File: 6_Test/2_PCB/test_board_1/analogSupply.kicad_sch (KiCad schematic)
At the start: 8 parts, among them U1 TPS74501PDRVR, U2 ADA4807-2ARMZ, U3 3310Y-001-103L

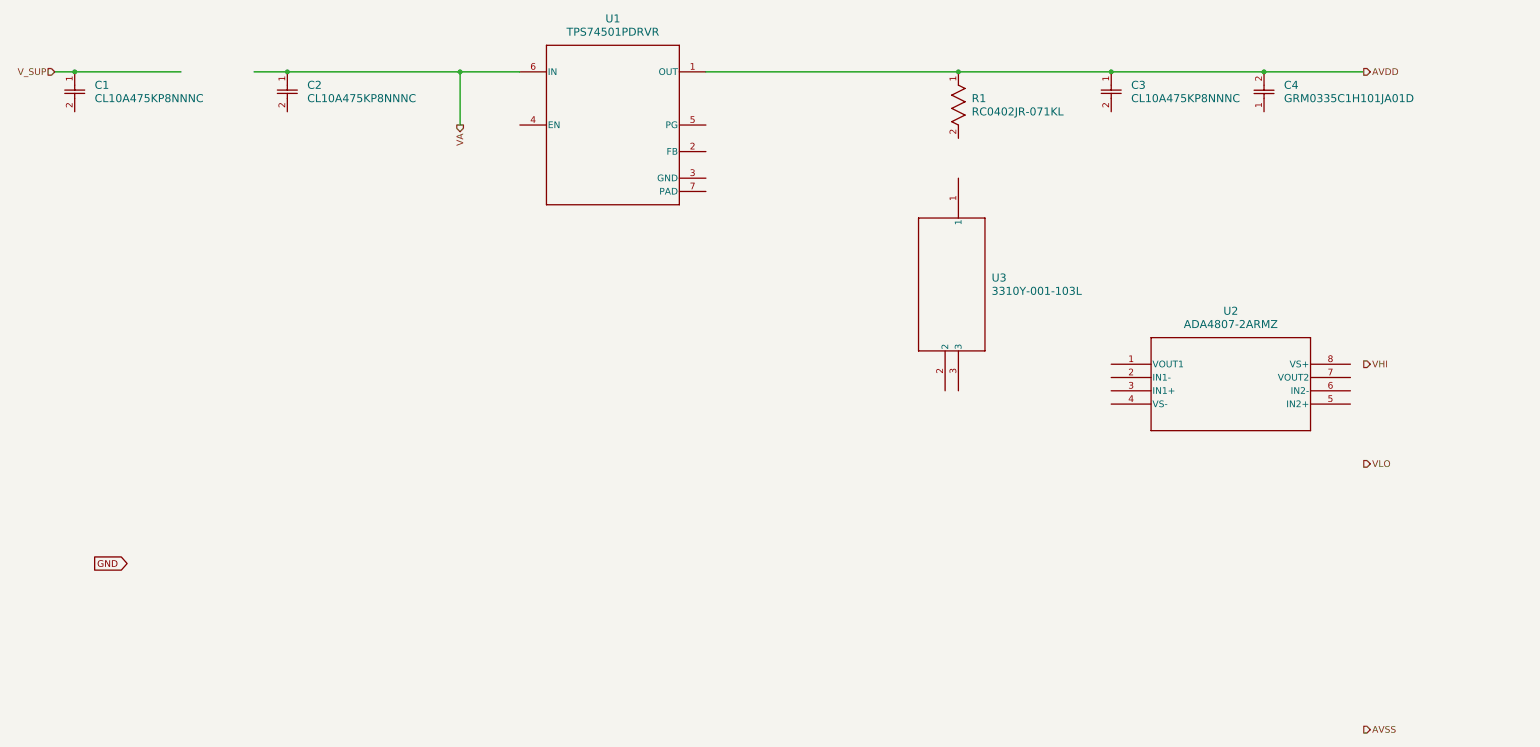
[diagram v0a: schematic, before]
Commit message: progress on analog supply
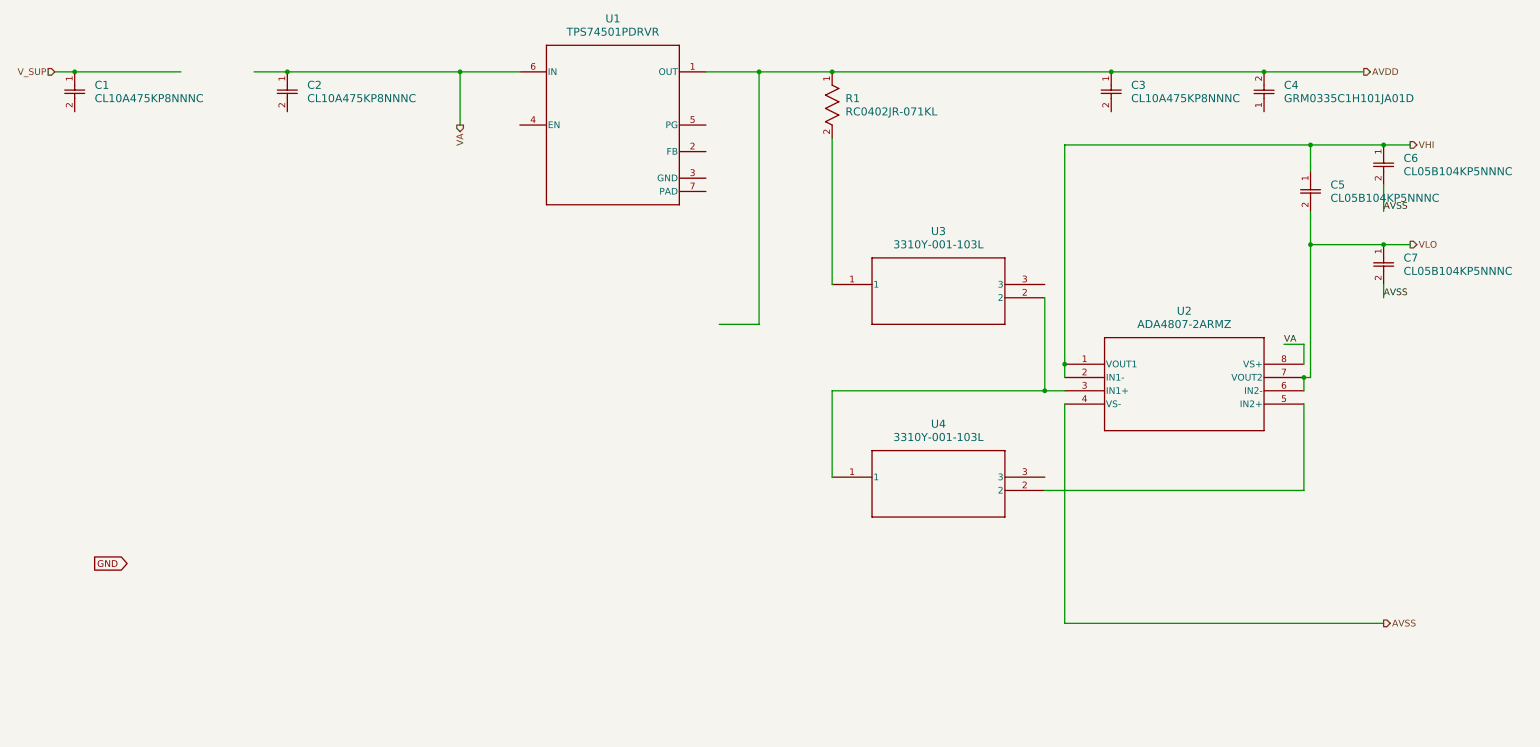
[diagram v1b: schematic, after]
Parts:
- added C5, C6, C7: CL05B104KP5NNNC, CAP_CL05_SAM, symbol cap100nF:CL05B104KP5NNNC
- added U4: 3310Y-001-103L, TO_3310Y, symbol potentiometer:3310Y-001-103L
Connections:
- net AVSS: now also U2.4 (VS-), C6.2, C7.2
- net VA: now also U2.8 (VS+)
- net VHI: now also U2.1 (VOUT1), U2.2 (IN1-), C5.1, C6.1
- net VLO: now also U2.6 (IN2-), U2.7 (VOUT2), C5.2, C7.1
- net at U3.1: now also R1.2
- net at U3.2: now also U2.3 (IN1+), U4.1
- net at U2.5 (IN2+): now also U4.2
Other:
- moved on the sheet: R1, U2, U3

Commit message: progress on analog supply. added ferrite beads
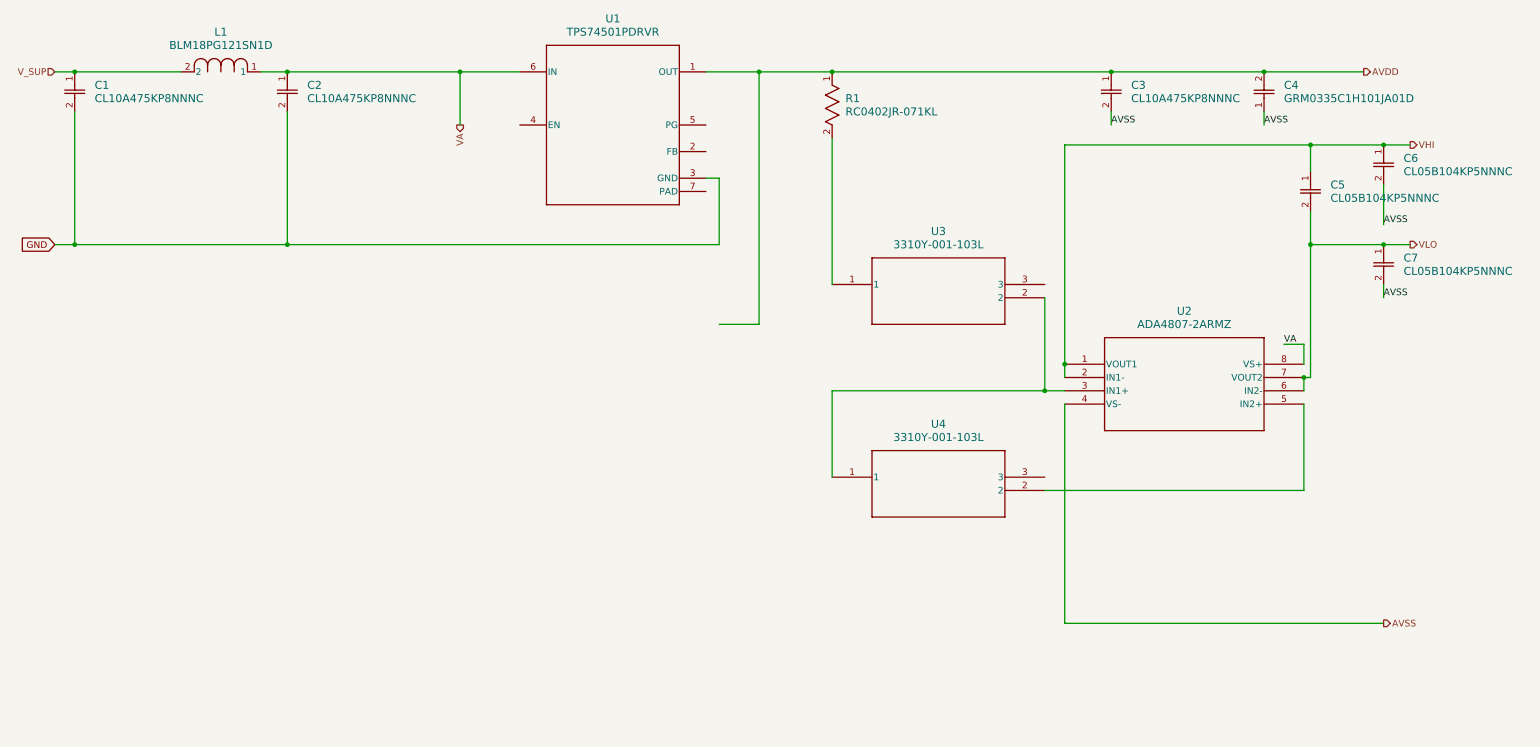
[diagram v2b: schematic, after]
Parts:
- added L1: BLM18PG121SN1D, IND_BLM18_0603_MUR, symbol ferriteBeads120Ohm:BLM18PG121SN1D
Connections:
- net AVSS: now also C3.2, C4.1
- net GND: now also C1.2, C2.2, U1.3 (GND)
- net VA: now also L1.1
- net V_SUP: now also L1.2
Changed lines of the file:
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@@
 	(paper "A4")
 	(junction
+		(at 26.67 63.5)
+		(diameter 0)
+		(color 0 0 0 0)
+	)
+	(junction
 		(at 276.86 44.45)
 		(diameter 0)
@@
 	)
 	(junction
+		(at 100.33 30.48)
+		(diameter 0)
+		(color 0 0 0 0)
+	)
+	(junction
+		(at 276.86 63.5)
+		(diameter 0)
+		(color 0 0 0 0)
+	)
+	(junction
+		(at 67.31 63.5)
+		(diameter 0)
+		(color 0 0 0 0)
+	)
+	(junction
+		(at 171.45 30.48)
+		(diameter 0)
+		(color 0 0 0 0)
+	)
+	(junction
 		(at 67.31 30.48)
 		(diameter 0)
@@
 	)
 	(junction
-		(at 100.33 30.48)
-		(diameter 0)
-		(color 0 0 0 0)
-	)
-	(junction
-		(at 276.86 63.5)
-		(diameter 0)
-		(color 0 0 0 0)
-	)
-	(junction
-		(at 171.45 30.48)
-		(diameter 0)
-		(color 0 0 0 0)
-	)
-	(junction
 		(at 215.9 86.36)
 		(diameter 0)
@@
 	(wire
 		(pts
+			(xy 67.31 38.1) (xy 67.31 63.5)
+		)
+		(stroke
+			(width 0)
+			(type default)
+		)
+	)
+	(wire
+		(pts
 			(xy 22.86 30.48) (xy 26.67 30.48)
 		)
@@
 	(wire
 		(pts
+			(xy 149.86 63.5) (xy 67.31 63.5)
+		)
+		(stroke
+			(width 0)
+			(type default)
+		)
+	)
+	(wire
+		(pts
 			(xy 100.33 30.48) (xy 111.76 30.48)
 		)
@@
 	(wire
 		(pts
-			(xy 60.96 30.48) (xy 67.31 30.48)
+			(xy 26.67 38.1) (xy 26.67 63.5)
+		)
+		(stroke
+			(width 0)
+			(type default)
+		)
+	)
+	(wire
+		(pts
+			(xy 26.67 63.5) (xy 22.86 63.5)
+		)
+		(stroke
+			(width 0)
+			(type default)
+		)
+	)
+	(wire
+		(pts
+			(xy 224.79 38.1) (xy 224.79 40.64)
 		)
 		(stroke
@@
 	(wire
 		(pts
+			(xy 67.31 63.5) (xy 26.67 63.5)
+		)
+		(stroke
+			(width 0)
+			(type default)
+		)
+	)
+	(wire
+		(pts
 			(xy 26.67 30.48) (xy 46.99 30.48)
 		)
@@
 	(wire
 		(pts
+			(xy 149.86 50.8) (xy 149.86 63.5)
+		)
+		(stroke
+			(width 0)
+			(type default)
+		)
+	)
+	(wire
+		(pts
+			(xy 62.23 30.48) (xy 67.31 30.48)
+		)
+		(stroke
+			(width 0)
+			(type default)
+		)
+	)
+	(wire
+		(pts
+			(xy 147.32 50.8) (xy 149.86 50.8)
+		)
+		(stroke
+			(width 0)
+			(type default)
+		)
+	)
+	(wire
+		(pts
 			(xy 215.9 44.45) (xy 262.89 44.45)
 		)
@@
 	(wire
 		(pts
+			(xy 254 38.1) (xy 254 40.64)
+		)
+		(stroke
+			(width 0)
+			(type default)
+		)
+	)
+	(wire
+		(pts
 			(xy 224.79 30.48) (xy 254 30.48)
 		)
@@
 	(wire
 		(pts
+			(xy 276.86 52.07) (xy 276.86 59.69)
+		)
+		(stroke
+			(width 0)
+			(type default)
+		)
+	)
+	(wire
+		(pts
 			(xy 262.89 63.5) (xy 276.86 63.5)
 		)
@@
 	(wire
 		(pts
-			(xy 276.86 52.07) (xy 276.86 57.15)
-		)
-		(stroke
-			(width 0)
-			(type default)
-		)
-	)
-	(wire
-		(pts
 			(xy 261.62 88.9) (xy 261.62 91.44)
 		)
@@
 			(width 0)
 			(type default)
+		)
+	)
+	(label "AVSS"
+		(at 224.79 40.64 0)
+		(fields_autoplaced yes)
+		(effects
+			(font
+				(size 1.27 1.27)
+			)
+			(justify left bottom)
 		)
 	)
@@
 	)
 	(label "AVSS"
-		(at 276.86 57.15 0)
+		(at 254 40.64 0)
 		(fields_autoplaced yes)
 		(effects
@@
 		)
 	)
+	(label "AVSS"
+		(at 276.86 59.69 0)
+		(fields_autoplaced yes)
+		(effects
+			(font
+				(size 1.27 1.27)
+			)
+			(justify left bottom)
+		)
+	)
 	(global_label "GND"
-		(shape output)
-		(at 30.48 124.46 0)
-		(fields_autoplaced yes)
-		(effects
-			(font
-				(size 1.27 1.27)
-			)
-			(justify left)
+		(shape input)
+		(at 22.86 63.5 180)
+		(fields_autoplaced yes)
+		(effects
+			(font
+				(size 1.27 1.27)
+			)
+			(justify right)
 		)
 		(property "Intersheetrefs" "${INTERSHEET_REFS}"
-			(at 37.3357 124.46 0)
+			(at 16.0043 63.5 0)
 			(effects
 				(font
 					(size 1.27 1.27)
 				)
-				(justify left)
+				(justify right)
 				(hide yes)
 			)
@@
 					(unit 1)
 				)
+			)
+		)
+	)
+	(symbol
+		(lib_id "ferriteBeads120Ohm:BLM18PG121SN1D")
+		(at 46.99 30.48 0)
+		(unit 1)
+		(exclude_from_sim no)
+		(in_bom yes)
+		(on_board yes)
+		(dnp no)
+		(fields_autoplaced yes)
+		(property "Reference" "L1"
+			(at 54.61 22.86 0)
+			(effects
+				(font
+					(size 1.524 1.524)
+				)
+			)
+		)
+		(property "Value" "BLM18PG121SN1D"
+			(at 54.61 25.4 0)
+			(effects
+				(font
+					(size 1.524 1.524)
+				)
+			)
+		)
+		(property "Footprint" "IND_BLM18_0603_MUR"
+			(at 46.99 30.48 0)
+			(effects
+				(font
+					(size 1.27 1.27)
+					(italic yes)
+				)
+				(hide yes)
+			)
+		)
+		(property "Datasheet" "BLM18PG121SN1D"
+			(at 46.99 30.48 0)
+			(effects
+				(font
+					(size 1.27 1.27)
+					(italic yes)
+				)
+				(hide yes)
+			)
+		)
+		(property "Description" ""
+			(at 46.99 30.48 0)
+			(effects
+				(font
+					(size 1.27 1.27)
+				)
+				(hide yes)
+			)
+		)
+		(pin "1"
+		)
+		(pin "2"
+		)
+		(instances
+			(project ""
+				(path "/7acc191a-fe8c-48a0-9d8b-f697ef59ac03/52b67f2c-cc8e-4f62-a575-3aba327208d6"
+					(reference "L1")
+					(unit 1)
+				)

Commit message: backups and testing lone schematics
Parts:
- removed C1, C2, C3: CL10A475KP8NNNC, CAP_0603_CL10A_1P6XP8_SAM, symbol cap4.7uF:CL10A475KP8NNNC
- removed C4: GRM0335C1H101JA01D, G-033_MUR, symbol cap100pF:GRM0335C1H101JA01D
- removed C5, C6, C7: CL05B104KP5NNNC, CAP_CL05_SAM, symbol cap100nF:CL05B104KP5NNNC
- removed L1: BLM18PG121SN1D, IND_BLM18_0603_MUR, symbol ferriteBeads120Ohm:BLM18PG121SN1D
- removed R1: RC0402JR-071KL, RC0402N_YAG, symbol resistor1k:RC0402JR-071KL
- removed U1: TPS74501PDRVR, DRV0006A, symbol LDO:TPS74501PDRVR
- removed U2: ADA4807-2ARMZ, RM-8_ADI, symbol opAmp:ADA4807-2ARMZ
- removed U3, U4: 3310Y-001-103L, TO_3310Y, symbol potentiometer:3310Y-001-103L
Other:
- added sheet FerriteBeads (ferriteBeads.kicad_sch)
- added sheet LDO (ldo.kicad_sch)
